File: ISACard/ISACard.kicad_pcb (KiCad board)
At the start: 2 copper layers, 189.7 x 95.9 mm, 104 parts, among them J1 Bus_ISA_8bit, J2 ICSP, J3 EXTSPI, J4 SERCON, J5 Conn_01x16, Q1 2N3904, Q2 2N3906, SW1 SW_Push, U1 74LS86, U10 28C256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

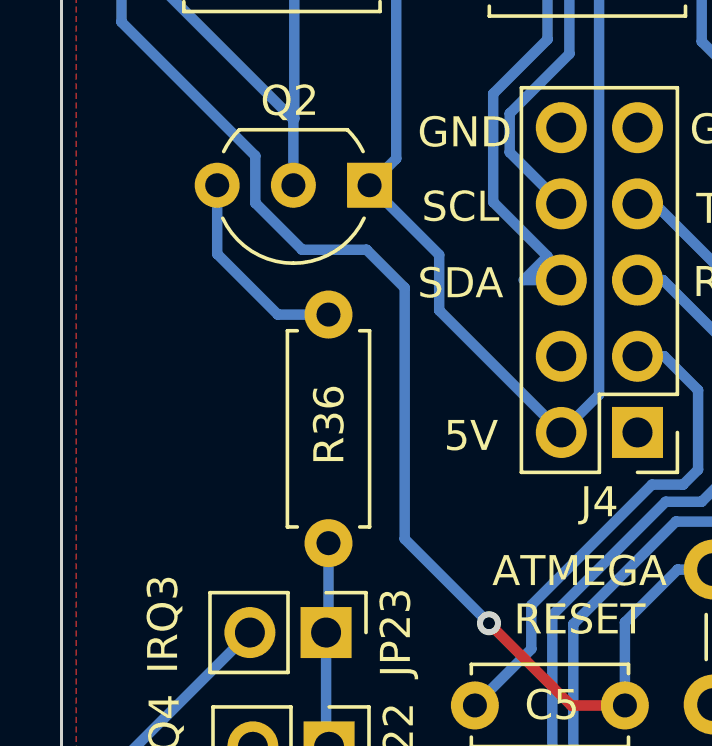
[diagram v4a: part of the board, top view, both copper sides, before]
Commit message: Adjusted bias of resistors
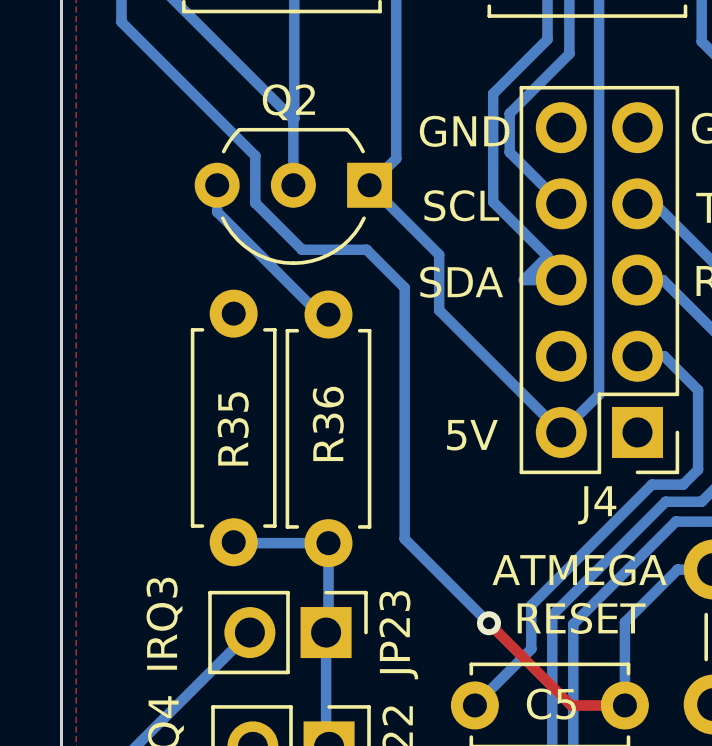
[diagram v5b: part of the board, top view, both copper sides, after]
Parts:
- added R35: 22k, Resistor_THT:R_Axial_DIN0207_L6.3mm_D2.5mm_P7.62mm_Horizontal, F.Cu at (56.7, 85.0)
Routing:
- net Net-(JP16-A): track 14.4 -> 17.6 mm
- net Net-(Q2-C): track 6.84 -> 6.02 mm
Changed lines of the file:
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@@
     )
   )
+  (footprint "Resistor_THT:R_Axial_DIN0207_L6.3mm_D2.5mm_P7.62mm_Horizontal" (layer "F.Cu")
+    (at 56.72 85.03 90)
+    (descr "Resistor, Axial_DIN0207 series, Axial, Horizontal, pin pitch=7.62mm, 0.25W = 1/4W, length*diameter=6.3*2.5mm^2, http://cdn-reichelt.de/documents/datenblatt/B400/1_4W%23YAG.pdf")
+    (tags "Resistor Axial_DIN0207 series Axial Horizontal pin pitch 7.62mm 0.25W = 1/4W length 6.3mm diameter 2.5mm")
+    (property "Sheetfile" "ISACard.kicad_sch")
+    (property "Sheetname" "")
+    (property "ki_description" "Resistor")
+    (property "ki_keywords" "R res resistor")
+    (attr through_hole)
+    (fp_text reference "R35" (at 3.77 0.02 90) (layer "F.SilkS")
+        (effects (font (size 1 1) (thickness 0.15)))
+    )
+    (fp_text value "22k" (at 3.81 2.37 90) (layer "F.Fab")
+        (effects (font (size 1 1) (thickness 0.15)))
+    )
+    (fp_text user "${REFERENCE}" (at 3.81 0 90) (layer "F.Fab")
+        (effects (font (size 1 1) (thickness 0.15)))
+    )
+    (fp_line (start 0.54 -1.37) (end 7.08 -1.37)
+      (stroke (width 0.12) (type solid)) (layer "F.SilkS"))
+    (fp_line (start 0.54 -1.04) (end 0.54 -1.37)
+      (stroke (width 0.12) (type solid)) (layer "F.SilkS"))
+    (fp_line (start 0.54 1.04) (end 0.54 1.37)
+      (stroke (width 0.12) (type solid)) (layer "F.SilkS"))
+    (fp_line (start 0.54 1.37) (end 7.08 1.37)
+      (stroke (width 0.12) (type solid)) (layer "F.SilkS"))
+    (fp_line (start 7.08 -1.37) (end 7.08 -1.04)
+      (stroke (width 0.12) (type solid)) (layer "F.SilkS"))
+    (fp_line (start 7.08 1.37) (end 7.08 1.04)
+      (stroke (width 0.12) (type solid)) (layer "F.SilkS"))
+    (fp_line (start -1.05 -1.5) (end -1.05 1.5)
+      (stroke (width 0.05) (type solid)) (layer "F.CrtYd"))
+    (fp_line (start -1.05 1.5) (end 8.67 1.5)
+      (stroke (width 0.05) (type solid)) (layer "F.CrtYd"))
+    (fp_line (start 8.67 -1.5) (end -1.05 -1.5)
+      (stroke (width 0.05) (type solid)) (layer "F.CrtYd"))
+    (fp_line (start 8.67 1.5) (end 8.67 -1.5)
+      (stroke (width 0.05) (type solid)) (layer "F.CrtYd"))
+    (fp_line (start 0 0) (end 0.66 0)
+      (stroke (width 0.1) (type solid)) (layer "F.Fab"))
+    (fp_line (start 0.66 -1.25) (end 0.66 1.25)
+      (stroke (width 0.1) (type solid)) (layer "F.Fab"))
+    (fp_line (start 0.66 1.25) (end 6.96 1.25)
+      (stroke (width 0.1) (type solid)) (layer "F.Fab"))
+    (fp_line (start 6.96 -1.25) (end 0.66 -1.25)
+      (stroke (width 0.1) (type solid)) (layer "F.Fab"))
+    (fp_line (start 6.96 1.25) (end 6.96 -1.25)
+      (stroke (width 0.1) (type solid)) (layer "F.Fab"))
+    (fp_line (start 7.62 0) (end 6.96 0)
+      (stroke (width 0.1) (type solid)) (layer "F.Fab"))
+    (pad "1" thru_hole circle (at 0 0 90) (size 1.6 1.6) (drill 0.8) (layers "*.Cu" "*.Mask")
+      (net 172 "Net-(JP16-A)") (pintype "passive"))
+    (pad "2" thru_hole oval (at 7.62 0 90) (size 1.6 1.6) (drill 0.8) (layers "*.Cu" "*.Mask")
+      (net 26 "GND") (pintype "passive"))
+    (model "${KICAD6_3DMODEL_DIR}/Resistor_THT.3dshapes/R_Axial_DIN0207_L6.3mm_D2.5mm_P7.62mm_Horizontal.wrl"
+      (offset (xyz 0 0 0))
+      (scale (xyz 1 1 1))
+      (rotate (xyz 0 0 0))
+    )
+  )
   (footprint "Package_TO_SOT_THT:TO-92_Inline_Wide" (layer "F.Cu")
     (at 61.25 73.13 180)
@@
   (segment (start 59.9 99.4) (end 59.9 95.71) (width 0.35) (layer "B.Cu") (net 172))
   (segment (start 59.88 87.96) (end 59.8 88.04) (width 0.35) (layer "B.Cu") (net 172))
+  (segment (start 56.75 85.06) (end 56.72 85.03) (width 0.35) (layer "B.Cu") (net 172))
   (segment (start 59.9 95.71) (end 59.89 95.7) (width 0.35) (layer "B.Cu") (net 172))
+  (segment (start 59.88 85.06) (end 56.75 85.06) (width 0.35) (layer "B.Cu") (net 172))
   (segment (start 59.8 88.04) (end 59.8 91.75) (width 0.35) (layer "B.Cu") (net 172))
   (segment (start 58.71 70.94) (end 54.518 66.748) (width 0.35) (layer "B.Cu") (net 173))
@@
   (segment (start 60.92 64.29) (end 58.74 66.47) (width 0.35) (layer "B.Cu") (net 173))
   (segment (start 64.7 66.12) (end 64.7 65.64) (width 0.35) (layer "B.Cu") (net 173))
-  (segment (start 58.19 77.44) (end 56.17 75.42) (width 0.35) (layer "B.Cu") (net 174))
-  (segment (start 59.88 77.44) (end 58.19 77.44) (width 0.35) (layer "B.Cu") (net 174))
-  (segment (start 56.17 75.42) (end 56.17 73.13) (width 0.35) (layer "B.Cu") (net 174))
+  (segment (start 56.17 74.02) (end 56.17 73.13) (width 0.35) (layer "B.Cu") (net 174))
+  (segment (start 59.59 77.44) (end 56.17 74.02) (width 0.35) (layer "B.Cu") (net 174))
+  (segment (start 59.88 77.44) (end 59.59 77.44) (width 0.35) (layer "B.Cu") (net 174))
   (zone (net 26) (net_name "GND") (layer "F.Cu") (hatch edge 0.5)
     (connect_pads (clearance 0.508))

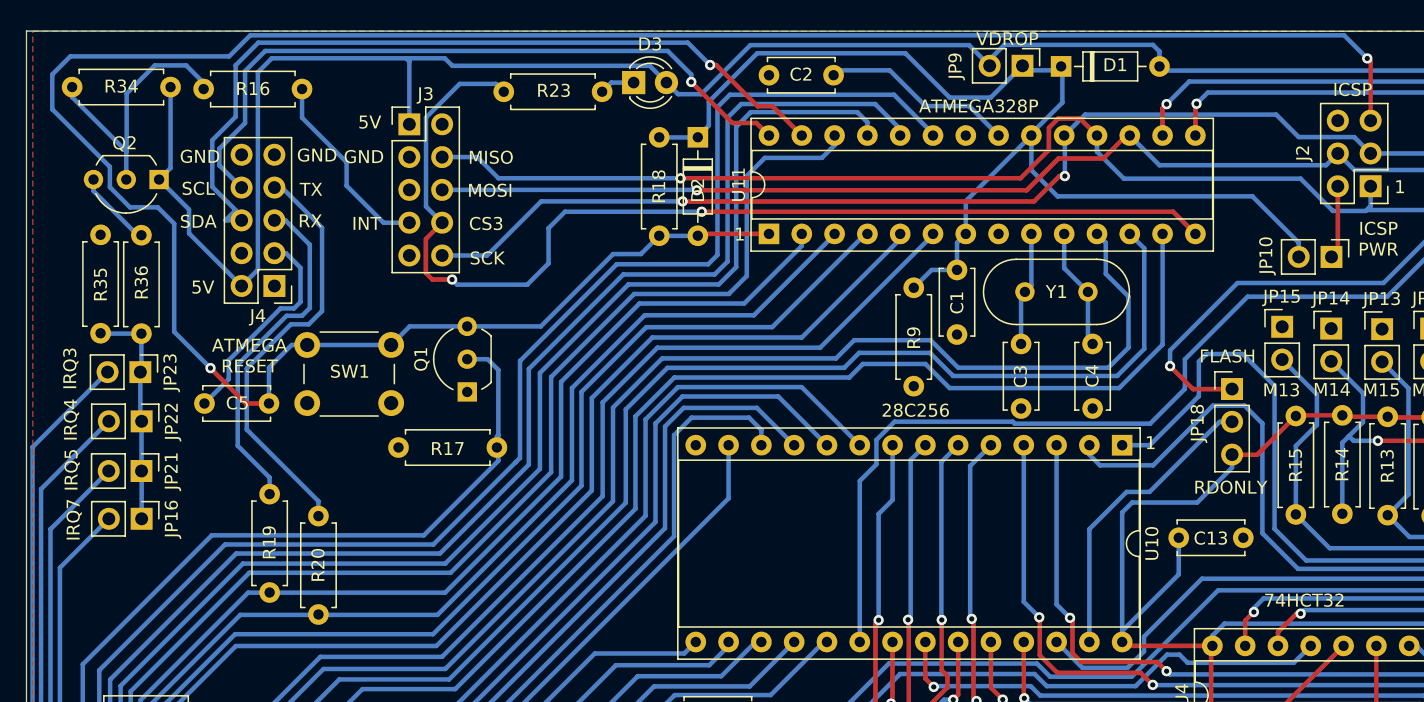
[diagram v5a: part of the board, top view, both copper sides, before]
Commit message: modified IRQ system
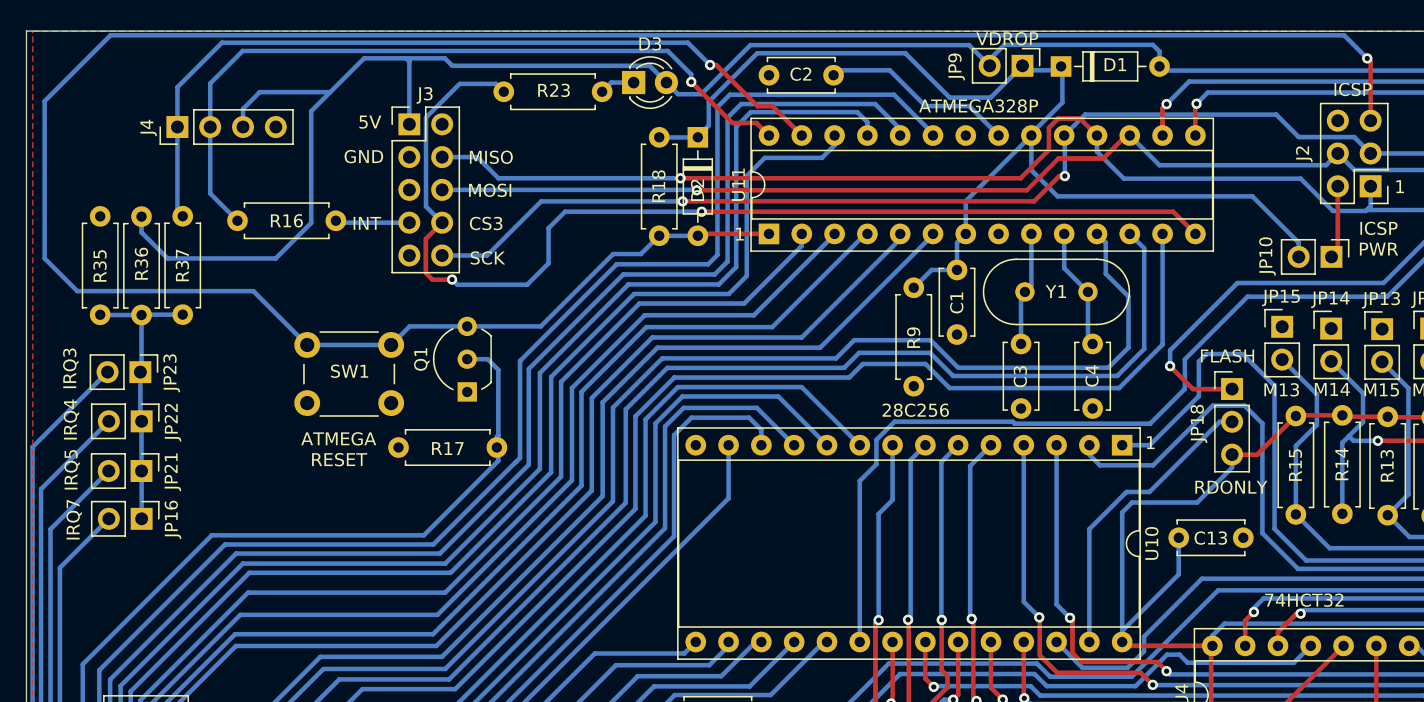
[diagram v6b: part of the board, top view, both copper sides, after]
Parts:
- removed C5: 100 nF, Capacitor_THT:C_Disc_D5.0mm_W2.5mm_P5.00mm
- removed Q2: 2N3906, Package_TO_SOT_THT:TO-92_Inline_Wide
- removed R19, R20: 2k2, Resistor_THT:R_Axial_DIN0207_L6.3mm_D2.5mm_P7.62mm_Horizontal
- removed R34: 100k, Resistor_THT:R_Axial_DIN0207_L6.3mm_D2.5mm_P7.62mm_Horizontal
- added R37: 1k, Resistor_THT:R_Axial_DIN0207_L6.3mm_D2.5mm_P7.62mm_Horizontal, F.Cu at (63.1, 76.0)
- J4: value SERCON -> Conn_01x04; footprint Connector_PinHeader_2.54mm:PinHeader_2x05_P2.54mm_Vertical -> Connector_PinHeader_2.54mm:PinHeader_1x04_P2.54mm_Vertical
- R16: value 10k -> 1k
- R36: value 1k -> NC
- moved J4 14.4 mm to (62.7, 69.1), turned to 90 degrees
- moved R16 10.5 mm to (74.9, 76.3)
- moved R36 1.44 mm to (59.9, 76.0)
- moved R35 1.43 mm to (56.7, 83.6)
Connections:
- J4 pad 1: unconnected-(J4-Pin_1-Pad1) -> APC4
- J4 pad 2: +5V -> APC5
- J4 pad 3: Net-(J4-Pin_3) -> +5V
- J4 pad 4: unconnected-(J4-Pin_4-Pad4) -> GND
- R16 pad 2: Net-(Q2-B) -> APC5
- R36 pad 1: Net-(Q2-C) -> +5V
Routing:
- net Net-(J4-Pin_7): track 32.8 -> 0.00 mm
- net Net-(J4-Pin_5): track 26.9 -> 0.00 mm
- net Net-(Q2-B): track 21.3 -> 0.00 mm
- net Net-(J4-Pin_3): track 16.7 -> 0.00 mm
- net INT: track 15.0 -> 5.75 mm
- net Net-(Q2-C): track 6.02 -> 0.00 mm
- net +5V: track 646.8 -> 642.2 mm
- net Net-(JP16-A): track 17.6 -> 22.3 mm
- net ARESET: track 189.3 -> 184.8 mm, vias 2 -> 1
- net APC5: track 54.8 -> 58.9 mm
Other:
- board text removed: "RX"
- board text removed: "SCL"
- board text removed: "SDA"
- board text removed: "TX"

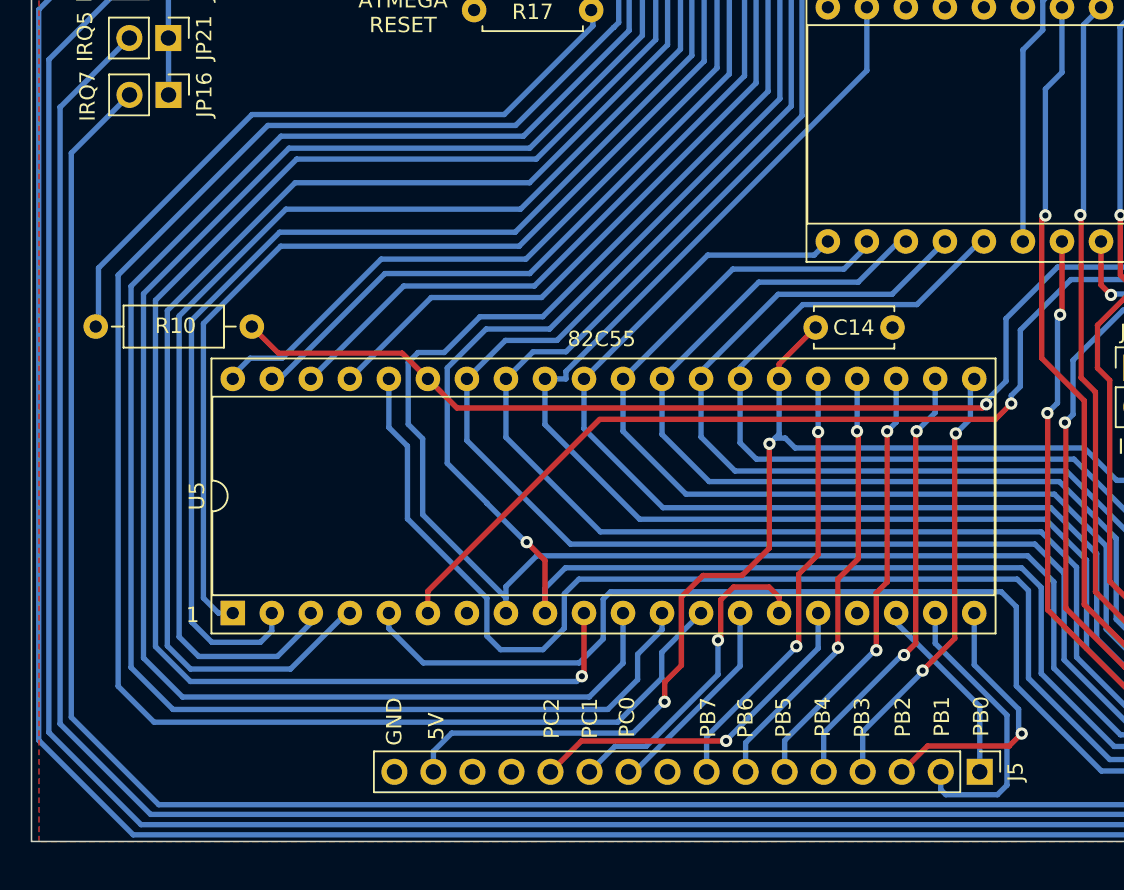
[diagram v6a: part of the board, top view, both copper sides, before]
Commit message: Added IRQ response bit to determine spurious interrupt
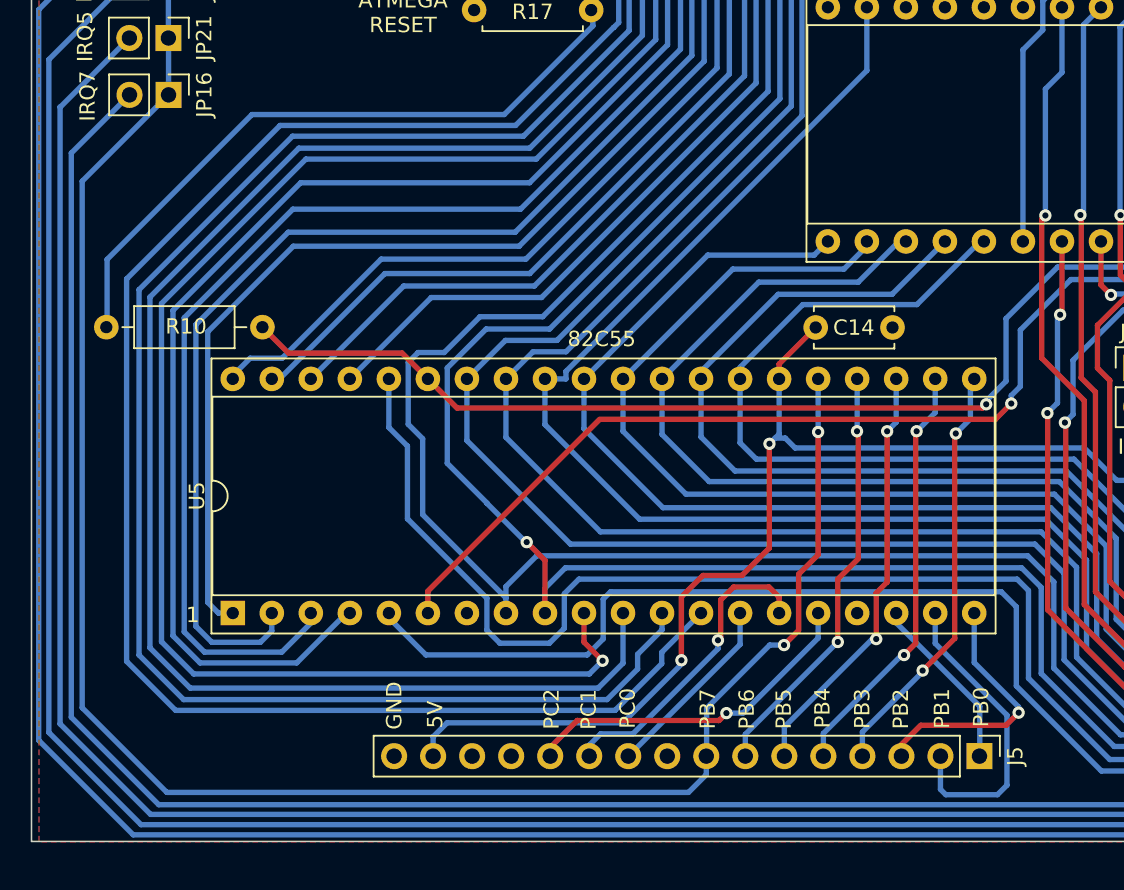
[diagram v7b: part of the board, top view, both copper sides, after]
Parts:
- moved J5 1.02 mm to (112.7, 142.4)
- moved R10 0.69 mm to (66.0, 114.5)
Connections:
- JP16 pad 1: Net-(JP16-A) -> PB7
- JP21 pad 1: Net-(JP16-A) -> PB7
- JP22 pad 1: Net-(JP16-A) -> PB7
- JP23 pad 1: Net-(JP16-A) -> PB7
- R35 pad 1: Net-(JP16-A) -> PB7
- R36 pad 2: Net-(JP16-A) -> PB7
- R37 pad 2: Net-(JP16-A) -> PB7
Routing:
- net PB7: track 28.6 -> 137.2 mm
- net Net-(JP16-A): track 22.3 -> 0.00 mm
- net PC4: track 165.1 -> 161.7 mm
- net PC5: track 156.5 -> 153.9 mm
- net PC6: track 148.5 -> 146.6 mm
- net PA0: track 106.8 -> 105.4 mm
- net +5V: track 642.2 -> 640.9 mm
- net PC0: track 13.6 -> 12.3 mm
- net PA1: track 103.8 -> 102.7 mm
- net PB2: track 18.0 -> 16.9 mm
- net PB1: track 19.0 -> 20.0 mm
- net PB6: track 28.7 -> 27.6 mm
- net PB3: track 28.6 -> 27.6 mm
- net PB0: track 12.6 -> 11.6 mm
- net PB4: track 28.7 -> 27.7 mm
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
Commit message: Send to JLCPCB
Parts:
- moved R11 1.57 mm to (213.0, 92.7)
- moved R16 1.56 mm to (73.4, 76.4)
- moved JP11 1.09 mm to (212.5, 84.3)
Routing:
- net INT: track 5.75 -> 7.27 mm
- net +5V: track 640.9 -> 640.2 mm
- net APC5: track 58.9 -> 58.3 mm
- net Net-(JP11-B): track 36.0 -> 35.4 mm
- net Net-(J2-Pin_2): vias 0 -> 1
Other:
- board text added: "+5V"
- board text added: "APC4"
- board text added: "APC5"
- board text added: "EXTSPI/ W5500"
- board text added: "PB7IRQ"
- board text added: "PC0/ BUSY"
- board text removed: "PB7"
- board text removed: "PC0"
